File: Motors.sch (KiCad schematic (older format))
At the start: 12 parts, among them J8 Conn_01x06_Female, J9 Conn_01x06_Female

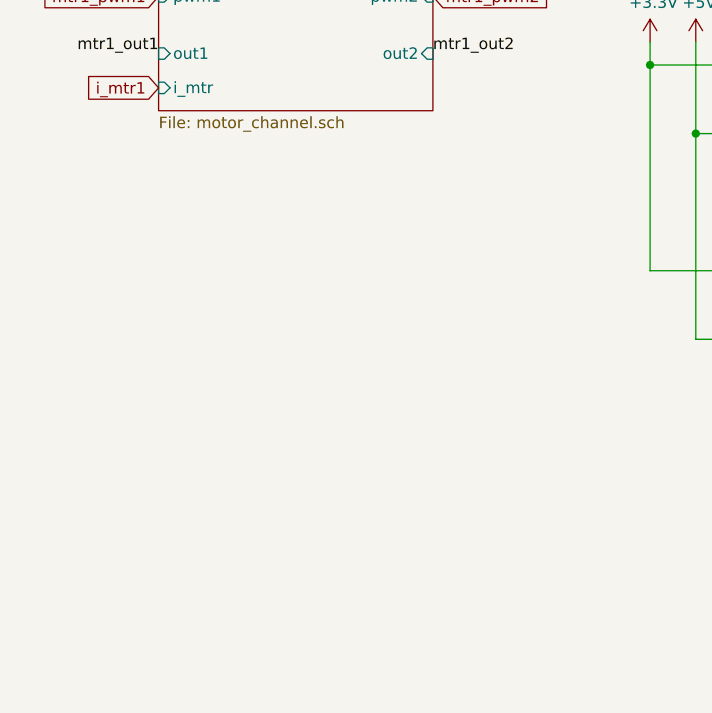
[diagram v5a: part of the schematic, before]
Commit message: added bldc channel
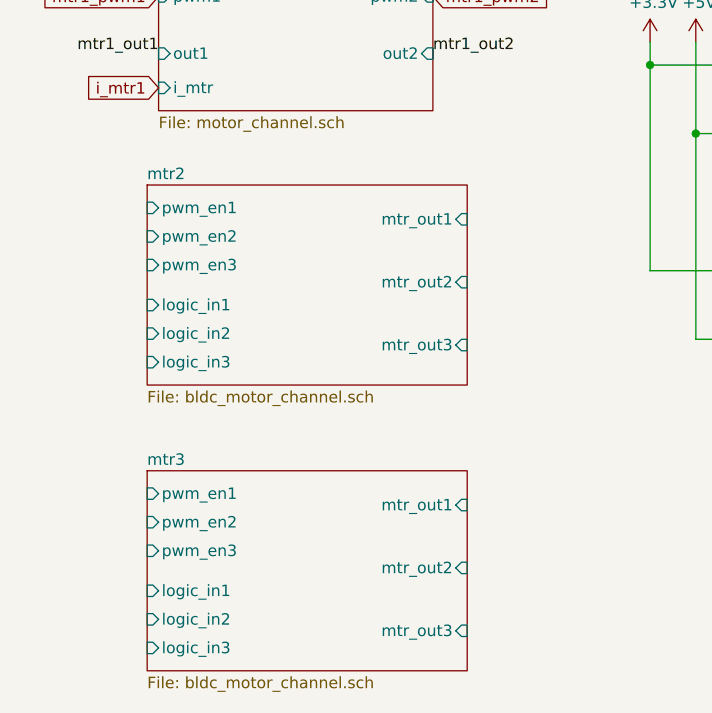
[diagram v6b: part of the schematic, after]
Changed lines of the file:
@@
 $Descr A4 11693 8268
 encoding utf-8
-Sheet 10 12
+Sheet 10 14
 Title ""
 Date ""
@@
 	0    1    1    0
 $EndComp
+$Sheet
+S 3500 4475 1400 875
+U 5E9A6A99
+F0 "mtr3" 50
+F1 "bldc_motor_channel.sch" 50
+F2 "pwm_en1" I L 3500 4575 50
+F3 "pwm_en2" I L 3500 4700 50
+F4 "pwm_en3" I L 3500 4825 50
+F5 "logic_in1" I L 3500 5000 50
+F6 "logic_in2" I L 3500 5125 50
+F7 "logic_in3" I L 3500 5250 50
+F8 "mtr_out1" I R 4900 4625 50
+F9 "mtr_out2" I R 4900 4900 50
+F10 "mtr_out3" I R 4900 5175 50
+$EndSheet
+$Sheet
+S 3500 3225 1400 875
+U 5E9A6A8E
+F0 "mtr2" 50
+F1 "bldc_motor_channel.sch" 50
+F2 "pwm_en1" I L 3500 3325 50
+F3 "pwm_en2" I L 3500 3450 50
+F4 "pwm_en3" I L 3500 3575 50
+F5 "logic_in1" I L 3500 3750 50
+F6 "logic_in2" I L 3500 3875 50
+F7 "logic_in3" I L 3500 4000 50
+F8 "mtr_out1" I R 4900 3375 50
+F9 "mtr_out2" I R 4900 3650 50
+F10 "mtr_out3" I R 4900 3925 50
+$EndSheet
 $EndSCHEMATC
